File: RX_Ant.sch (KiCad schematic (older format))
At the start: 57 parts, among them J1 CONN_COAXIAL, J10 CONN_COAXIAL, J11 CONN_01X06, J12 CONN_01X05, J13 CONN_COAXIAL, J14 CONN_COAXIAL, J15 CONN_COAXIAL, J16 CONN_01X01, J17 CONN_01X01, J18 CONN_01X01, J19 CONN_01X01, J2 CONN_COAXIAL, J20 CONN_01X01, J21 CONN_01X01, J22 CONN_01X01, J23 CONN_01X01, J24 CONN_COAXIAL, J25 CONN_COAXIAL, J26 CONN_COAXIAL, J27 CONN_COAXIAL, J28 CONN_COAXIAL, J29 CONN_COAXIAL, J3 CONN_COAXIAL, J30 CONN_COAXIAL, J31 CONN_COAXIAL, J32 CONN_COAXIAL, J33 CONN_COAXIAL, J34 CONN_COAXIAL, J35 CONN_COAXIAL, J36 CONN_COAXIAL, J4 CONN_COAXIAL, J5 CONN_COAXIAL, J6 CONN_COAXIAL, J7 CONN_COAXIAL, J8 CONN_COAXIAL, J9 CONN_COAXIAL

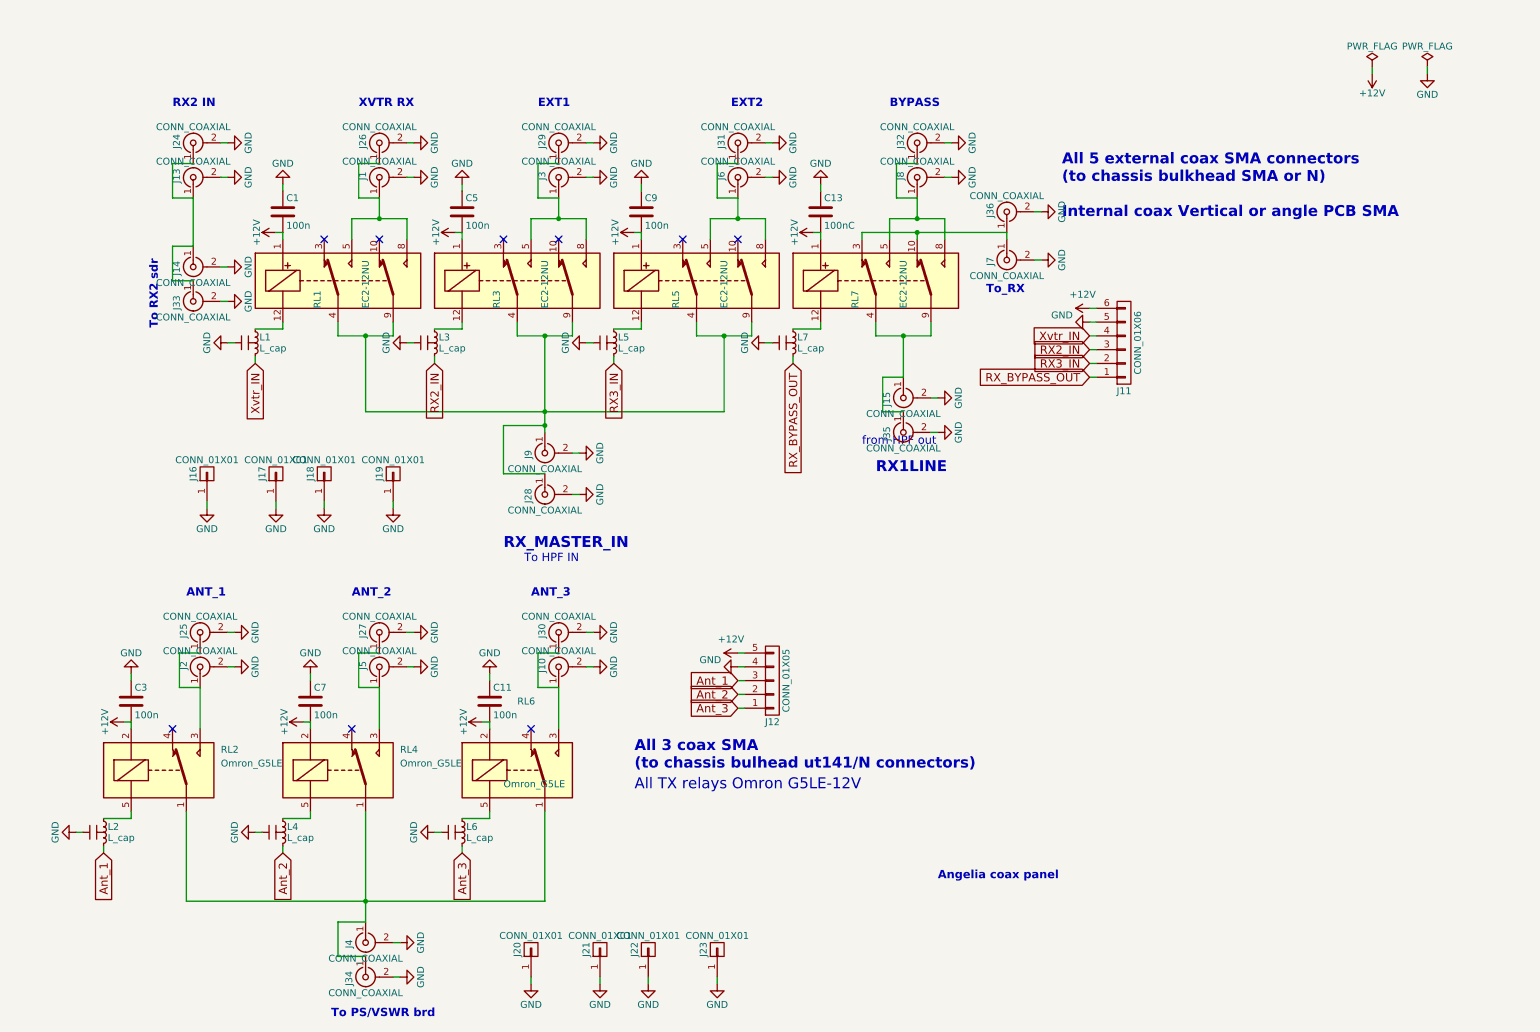
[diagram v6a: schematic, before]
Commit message: PS_In relay added, new routing V2
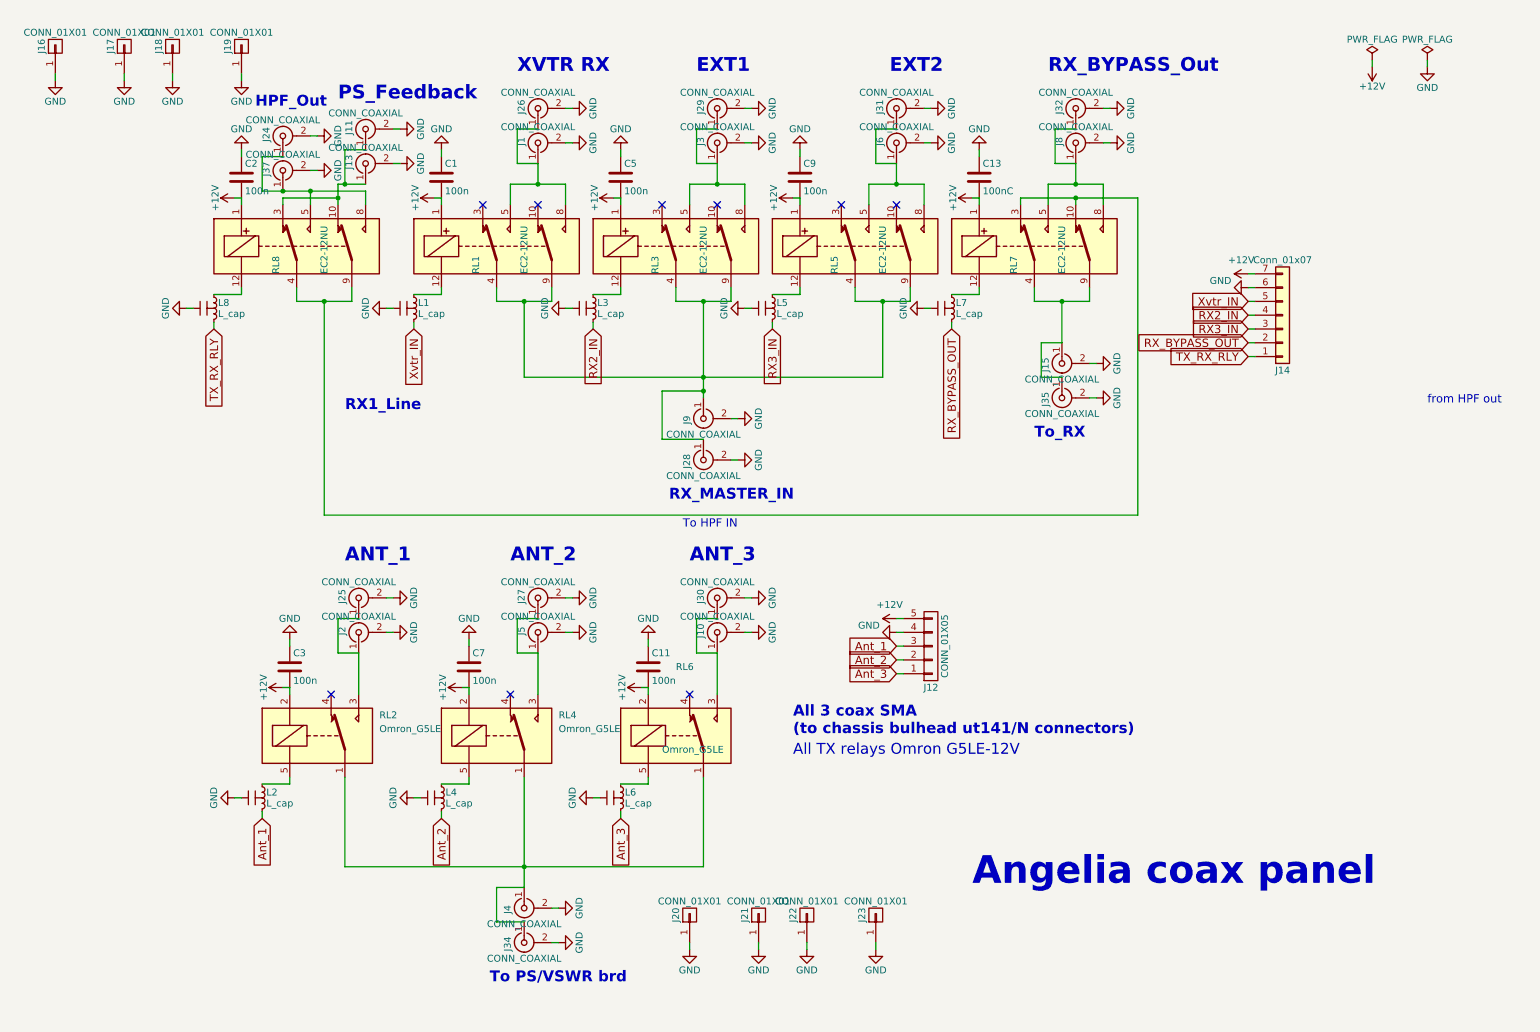
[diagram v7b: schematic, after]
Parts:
- removed J11: CONN_01X06, conn_kk100:kk100_22-23-2061, symbol CONN_01X06
- removed J14, J7: CONN_COAXIAL, conn_rf:sma_straight_32k101-400l5, symbol CONN_COAXIAL
- removed J33, J36: CONN_COAXIAL, Connector_Coaxial:SMA_Amphenol_132289_EdgeMount, symbol CONN_COAXIAL
- added C2: 100n, Capacitors_SMD:C_0805_HandSoldering, symbol C
- added J11: CONN_COAXIAL, Connector_Coaxial:SMA_Amphenol_132289_EdgeMount, symbol CONN_COAXIAL
- added J14: Conn_01x07, Connectors_Molex:Molex_KK-6410-07_07x2.54mm_Straight, symbol Conn_01x07
- added J37: CONN_COAXIAL, conn_rf:sma_straight_32k101-400l5, symbol CONN_COAXIAL
- added L8: L_cap, Ferrite_LC_NFM41P:Ferrite_LC_NFM41P, symbol L_cap
- added RL8: EC2-12NU, 2_Form_C_Relay:THT_2_formC, symbol EC2-12NU
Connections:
- net +12V: now also C2.2, J14.7 (Pin_7), RL8.1
- net GND: now also C2.1, J11.2 (Ext), J14.6 (Pin_6), J37.2 (Ext), L8.2
- net RX2_IN: now also J14.4 (Pin_4)
- net RX3_IN: now also J14.3 (Pin_3)
- net RX_BYPASS_OUT: now also J14.2 (Pin_2)
- net Xvtr_IN: now also J14.5 (Pin_5)
- net at RL7.10, RL7.3: now also RL8.4, RL8.9
- net at J13.1 (In): now also J11.1 (In), RL8.10, RL8.3; no longer J24.1 (In)
- new net: L8.1, RL8.12
- new net: J24.1 (In), J37.1 (In), RL8.5, RL8.8
- new net TX_RX_RLY: J14.1 (Pin_1), L8.3
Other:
- note added: "HPF_Out"
- note added: "PS_Feedback\n"
- note added: "RX1_Line"
- note added: "RX_BYPASS_Out"
- note removed: "All 5 external coax SMA connectors\n(to chassis bulkhead SMA or N)\n\nInternal coax Vertical or angle PCB SMA"
- note removed: "BYPASS"
- note removed: "RX2 IN"
- note removed: "To RX2 sdr\n"
- note removed: "\nRX1LINE"
- moved on the sheet: C1, C11, C13, C3, C5, C7, C9, J1, J10, J12, J15, J16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

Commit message: V3.0, RX_master connector added, new stitching
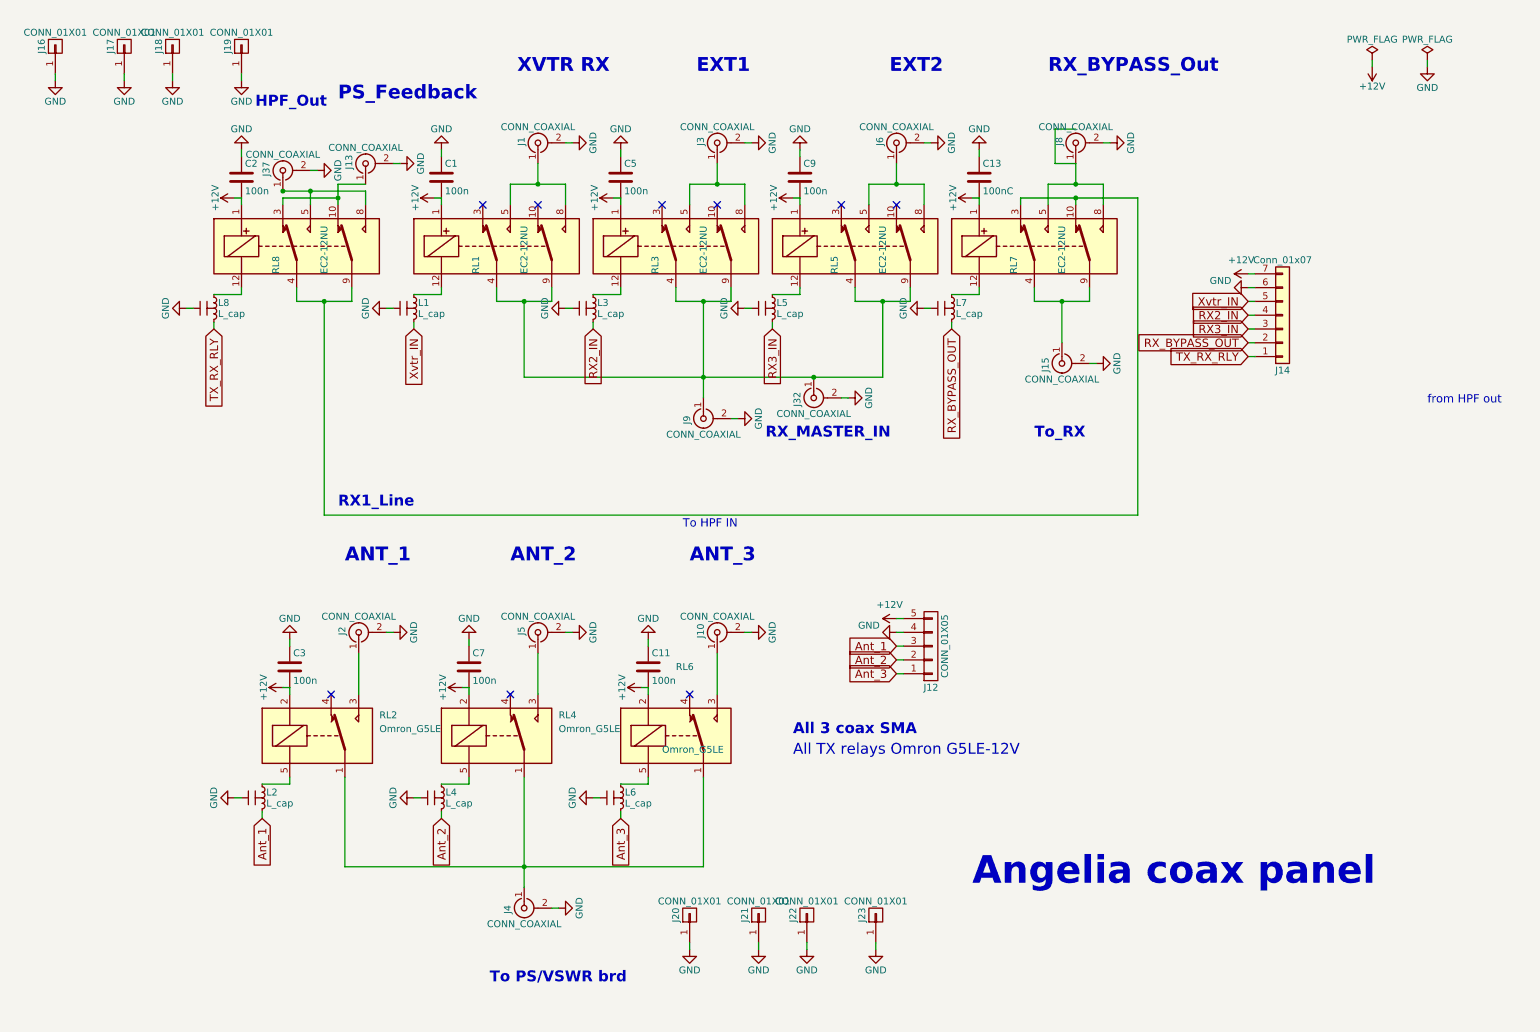
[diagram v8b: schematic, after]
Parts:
- removed J11, J24, J25, J26, J27, J28, J29, J30, J31, J34, J35: CONN_COAXIAL, Connector_Coaxial:SMA_Amphenol_132289_EdgeMount, symbol CONN_COAXIAL
- J32: footprint Connector_Coaxial:SMA_Amphenol_132289_EdgeMount -> conn_rf:sma_straight_32k101-400l5
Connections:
- net at J9.1 (In), RL1.4, RL1.9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: now also J32.1 (In)
- net at J8.1 (In), RL7.5, RL7.8: no longer J32.1 (In)
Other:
- note added: "All 3 coax SMA\n"
- note removed: "All 3 coax SMA\n(to chassis bulhead ut141/N connectors)"
- moved on the sheet: J32
